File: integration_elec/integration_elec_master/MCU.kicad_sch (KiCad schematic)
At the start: 0 parts

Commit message: EM - Ajout des pages hiérarchiques pour le master, next : ajouter connecteurs pour les capteurs
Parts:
- added C1 (x2), C3 (x2), C5, C6, C7, C8, C9: 0.10uF, Capacitor_SMD:C_0805_2012Metric_Pad1.18x1.45mm_HandSolder, symbol Device:C_Small
- added C10: 4.7uF, Capacitor_SMD:C_0805_2012Metric_Pad1.18x1.45mm_HandSolder, symbol Device:C_Small
- added C11, C12: 10pF, Capacitor_SMD:C_0805_2012Metric_Pad1.18x1.45mm_HandSolder, symbol Device:C_Small
- added L1: FerritBead 600 OHM, Inductor_SMD:L_0805_2012Metric_Pad1.15x1.40mm_HandSolder, symbol Device:FerriteBead
- added R2, R3, R38: 10k, Resistor_SMD:R_0805_2012Metric_Pad1.20x1.40mm_HandSolder, symbol Device:R_US
- added R37: 120, Resistor_SMD:R_0805_2012Metric_Pad1.20x1.40mm_HandSolder, symbol Device:R_US
- added SW1: SW_Push, Button_Switch_SMD:SW_SPST_TL3342, symbol Switch:SW_Push
- added U3: STM32F446RETx, Package_QFP:LQFP-64_10x10mm_P0.5mm, symbol MCU_ST_STM32F4:STM32F446RETx
- added Y1: Crystal_16MHz, ab2_xtal:CSM-3X, symbol Device:Crystal
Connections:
- new net: R37.1, SW1.1
- new net: C10.2, C9.2, U3.30 (VCAP_1)
- new net: R2.1, U3.60 (BOOT0)
- new net: C6.2, L1.2, U3.13 (VDDA)
- new net: C11.1, U3.5 (PH0), Y1.1
- new net: C12.1, U3.6 (PH1), Y1.2
- new net: R3.2, U3.34 (PB13)
- new net +3V3: C1.1, C1.1, C3.1, C3.1, C5.1, C7.1, L1.1, R38.1, U3.1 (VBAT), U3.19 (VDD), U3.32 (VDD), U3.48 (VDD), U3.64 (VDD)
- new net DEBUG_NJTRST: U3.56 (PB4)
- new net DEBUG_RESET: C8.1, R38.2, SW1.2, U3.7 (NRST)
- new net DEBUG_SWCLK_TCK: U3.49 (PA14)
- new net DEBUG_SWDIO_TMS: U3.46 (PA13)
- new net DEBUG_SWO_TDI: U3.50 (PA15)
- new net DEBUG_SWO_TDO: U3.55 (PB3)
- new net DEBUG_UART_RX: U3.25 (PC5)
- new net DEBUG_UART_TX: U3.29 (PB10)
- new net GND: C1.2, C1.2, C10.1, C11.2, C12.2, C3.2, C3.2, C5.2, C6.1, C7.2, C8.2, C9.1, R2.2, R37.2, U3.12 (VSSA), U3.18 (VSS), U3.31 (VSS), U3.47 (VSS), U3.63 (VSS)
- new net RF.XBEE_LED: U3.24 (PC4)
- new net RF.XBEE_RQ: U3.41 (PA8)
- new net RF.XBEE_UART_CTS: U3.44 (PA11)
- new net RF.XBEE_UART_IN: U3.42 (PA9)
- new net RF.XBEE_UART_OUT: U3.43 (PA10)
- new net RF.XBEE_UART_RTS: U3.45 (PA12)
- new net USB_D+: U3.36 (PB15)
- new net USB_D-: U3.35 (PB14)
- new net USB_ID: U3.33 (PB12)
- new net USB_VBUS: R3.1
- no-connect marks 0 -> 5
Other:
- note added: "If the flash is blank, the bootloader will enable."
- note added: "RESET"
- note added: "Stabilization for the main regulator"

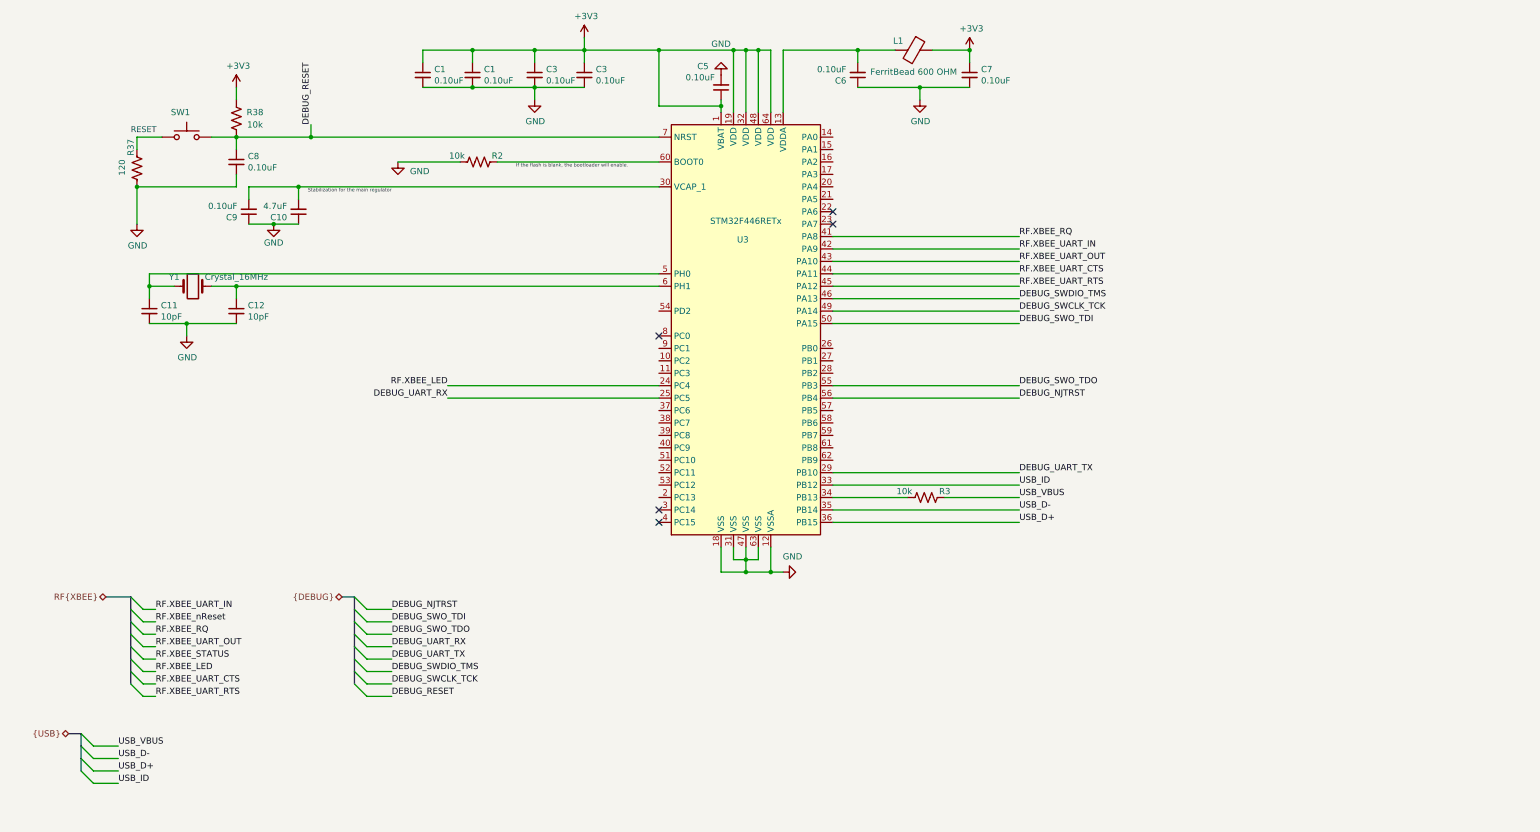
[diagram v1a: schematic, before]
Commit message: Added screen into schematic
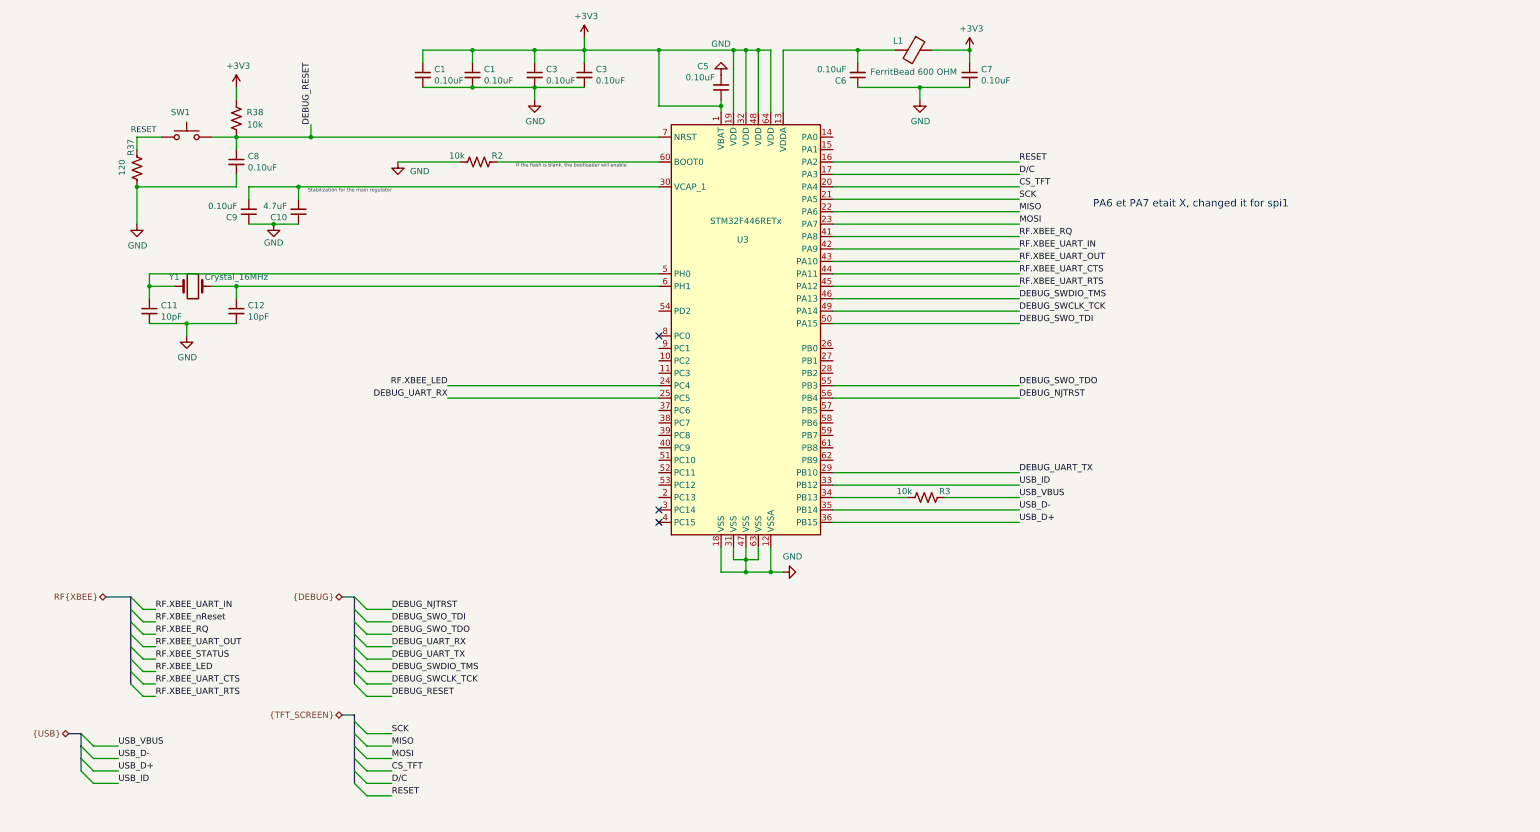
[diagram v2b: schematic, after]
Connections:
- net RESET: now reaches U3.16 (PA2)
- net D/C: now reaches U3.17 (PA3)
- net CS_TFT: now reaches U3.20 (PA4)
- net SCK: now reaches U3.21 (PA5)
- net MISO: now reaches U3.22 (PA6)
- net MOSI: now reaches U3.23 (PA7)
- no-connect marks 5 -> 3
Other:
- note added: "PA6 et PA7 etait X, changed it for spi1"

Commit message: Added footprint, symbol, 3D model for joystick. Added schematic for Joystick and comments
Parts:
- renumbered C1 to C11, C1 to C12, C3 to C13, C3 to C14, C5 to C15, C6 to C16, C7 to C17, C11 to C6, C8 to C7, C12 to C8, R37 to R5, R38 to R6, R2 to R7, R3 to R8, U3 to U2
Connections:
- net X_VALUE: now reaches U2.14 (PA0)
- net Y_VALUE: now reaches U2.15 (PA1)
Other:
- note added: "<- COULD BE PUT ON THE RESET, MIGHT BE BETTER..."

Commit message: Added plein de footprint
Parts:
- L1: footprint Inductor_SMD:L_0805_2012Metric_Pad1.15x1.40mm_HandSolder -> Inductor_SMD:L_0805_2012Metric_Pad1.05x1.20mm_HandSolder
- Y1: footprint ab2_xtal:CSM-3X -> JOYSTICK:XTAL_ECS-160-20-3X-TR
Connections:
- net VALVE_1: now reaches U2.39 (PC8)
- net VALVE_2: now reaches U2.40 (PC9)
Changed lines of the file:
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@@
 	)
 	(bus_entry
+		(at 30.48 138.43)
+		(size 2.54 2.54)
+		(stroke
+			(width 0)
+			(type default)
+		)
+	)
+	(bus_entry
 		(at 72.39 153.67)
 		(size 2.54 2.54)
@@
 	)
 	(bus_entry
-		(at 30.48 140.97)
+		(at 30.48 133.35)
 		(size 2.54 2.54)
 		(stroke
@@
 	)
 	(bus_entry
-		(at 30.48 143.51)
+		(at 30.48 135.89)
 		(size 2.54 2.54)
 		(stroke
@@
 	)
 	(bus_entry
+		(at 30.48 140.97)
+		(size 2.54 2.54)
+		(stroke
+			(width 0)
+			(type default)
+		)
+	)
+	(bus_entry
 		(at 72.39 161.29)
 		(size 2.54 2.54)
@@
 	(wire
 		(pts
+			(xy 102.87 114.3) (xy 146.05 114.3)
+		)
+		(stroke
+			(width 0)
+			(type default)
+		)
+	)
+	(wire
+		(pts
 			(xy 33.02 167.64) (xy 35.56 167.64)
 		)
@@
 	(wire
 		(pts
-			(xy 33.02 146.05) (xy 38.1 146.05)
+			(xy 33.02 138.43) (xy 38.1 138.43)
 		)
 		(stroke
@@
 	(wire
 		(pts
+			(xy 102.87 116.84) (xy 146.05 116.84)
+		)
+		(stroke
+			(width 0)
+			(type default)
+		)
+	)
+	(wire
+		(pts
 			(xy 33.02 154.94) (xy 35.56 154.94)
 		)
@@
 		)
 	)
+	(bus
+		(pts
+			(xy 30.48 138.43) (xy 30.48 140.97)
+		)
+		(stroke
+			(width 0)
+			(type default)
+		)
+	)
 	(wire
 		(pts
@@
 		)
 	)
+	(wire
+		(pts
+			(xy 33.02 140.97) (xy 38.1 140.97)
+		)
+		(stroke
+			(width 0)
+			(type default)
+		)
+	)
 	(bus
 		(pts
-			(xy 27.94 140.97) (xy 30.48 140.97)
+			(xy 27.94 133.35) (xy 30.48 133.35)
 		)
 		(stroke
@@
 	(wire
 		(pts
+			(xy 33.02 143.51) (xy 38.1 143.51)
+		)
+		(stroke
+			(width 0)
+			(type default)
+		)
+	)
+	(wire
+		(pts
 			(xy 74.93 151.13) (xy 80.01 151.13)
 		)
@@
 	(wire
 		(pts
-			(xy 33.02 143.51) (xy 38.1 143.51)
+			(xy 33.02 135.89) (xy 38.1 135.89)
 		)
 		(stroke
@@
 	(bus
 		(pts
-			(xy 30.48 140.97) (xy 30.48 143.51)
+			(xy 30.48 133.35) (xy 30.48 135.89)
 		)
 		(stroke
@@
 		)
 	)
+	(bus
+		(pts
+			(xy 30.48 135.89) (xy 30.48 138.43)
+		)
+		(stroke
+			(width 0)
+			(type default)
+		)
+	)
 	(wire
 		(pts
@@
 	)
 	(label "X_VALUE"
-		(at 38.1 143.51 0)
+		(at 38.1 135.89 0)
 		(effects
 			(font
@@
 		)
 	)
+	(label "VALVE_2"
+		(at 102.87 116.84 180)
+		(effects
+			(font
+				(size 1.27 1.27)
+			)
+			(justify right bottom)
+		)
+	)
 	(label "Y_VALUE"
-		(at 38.1 146.05 0)
+		(at 38.1 138.43 0)
 		(effects
 			(font
@@
 		)
 	)
+	(label "VALVE_1"
+		(at 102.87 114.3 180)
+		(effects
+			(font
+				(size 1.27 1.27)
+			)
+			(justify right bottom)
+		)
+	)
 	(label "DEBUG_SWCLK_TCK"
 		(at 219.71 88.9 0)
@@
 		)
 	)
+	(label "VALVE_1"
+		(at 38.1 140.97 0)
+		(effects
+			(font
+				(size 1.27 1.27)
+			)
+			(justify left bottom)
+		)
+	)
 	(label "DEBUG_UART_TX"
 		(at 219.71 121.92 0)
@@
 		)
 	)
+	(label "VALVE_2"
+		(at 38.1 143.51 0)
+		(effects
+			(font
+				(size 1.27 1.27)
+			)
+			(justify left bottom)
+		)
+	)
 	(label "DEBUG_SWDIO_TMS"
 		(at 219.71 86.36 0)
@@
 	(hierarchical_label "{JOYSTICK}"
 		(shape bidirectional)
-		(at 27.94 140.97 180)
+		(at 27.94 133.35 180)
 		(effects
 			(font
@@
 			)
 		)
-		(property "Footprint" "Inductor_SMD:L_0805_2012Metric_Pad1.15x1.40mm_HandSolder"
+		(property "Footprint" "Inductor_SMD:L_0805_2012Metric_Pad1.05x1.20mm_HandSolder"
 			(at 198.12 33.782 90)
 			(effects
@@
 			)
 		)
-		(property "Footprint" "ab2_xtal:CSM-3X"
+		(property "Footprint" "JOYSTICK:XTAL_ECS-160-20-3X-TR"
 			(at 50.8 83.82 0)
 			(effects

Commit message: Added comment for pull-down
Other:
- note added: "PC8 AND PC9 NEEDS TO BE PULL-DOWN"
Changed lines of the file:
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@@
 	(generator_version "9.0")
 	(paper "A4")
+	(text "PC8 AND PC9 NEEDS TO BE PULL-DOWN\n"
+		(exclude_from_sim no)
+		(at 69.596 114.554 0)
+		(effects
+			(font
+				(size 1.27 1.27)
+			)
+		)
+	)
 	(text "RESET"
 		(exclude_from_sim no)

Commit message: KAH - Fini schematic attente de review + correction BUS
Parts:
- added R10, R5: 0, Resistor_SMD:R_0805_2012Metric_Pad1.20x1.40mm_HandSolder, symbol Device:R_US
- renumbered R5 to R6, R6 to R7, R7 to R8, R8 to R9
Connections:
- net RF.XBEE_STATUS: now also U2.40 (PC9)
- net RF.XBEE_nReset: now also U2.51 (PC10)
- net VALVE_1: now also U2.38 (PC7); no longer U2.39 (PC8)
- net VALVE_2: now also U2.39 (PC8); no longer U2.40 (PC9)
- net at R6.1, SW1.1: now also R5.2
- net DEBUG_SWCLK_TCK renamed DEBUG_SWCLK
- net DEBUG_SWDIO_TMS renamed DEBUG_SWDIO
- net RESET: no longer names the net of U2.16 (PA2)
- net RESET: now also R10.1
- net USB_ID: no longer names the net of U2.33 (PB12)
- net X_VALUE: no longer names the net of U2.14 (PA0)
- net Y_VALUE: no longer names the net of U2.15 (PA1)
- new net RESET_TFT: R10.2, R5.1
- no-connect marks 3 -> 22

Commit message: KAH - added the part # for some pieces. MISSING R NC and USB-C conn
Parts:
- R10, R5: DigiKey (none) -> RMCF0805ZT0R00CT-ND
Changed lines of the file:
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@@
+			)
+		)
+		(property "DigiKey" "RMCF0805ZT0R00CT-ND"
+			(at 26.67 53.34 90)
+			(effects
+				(font
+					(size 1.27 1.27)
+				)
+				(hide yes)
 			)
 		)
@@
 			(effects
 				(font
+					(size 1.27 1.27)
+				)
+				(hide yes)
+			)
+		)
+		(property "DigiKey" "RMCF0805ZT0R00CT-ND"
+			(at 233.68 58.42 90)
+			(effects
+				(font

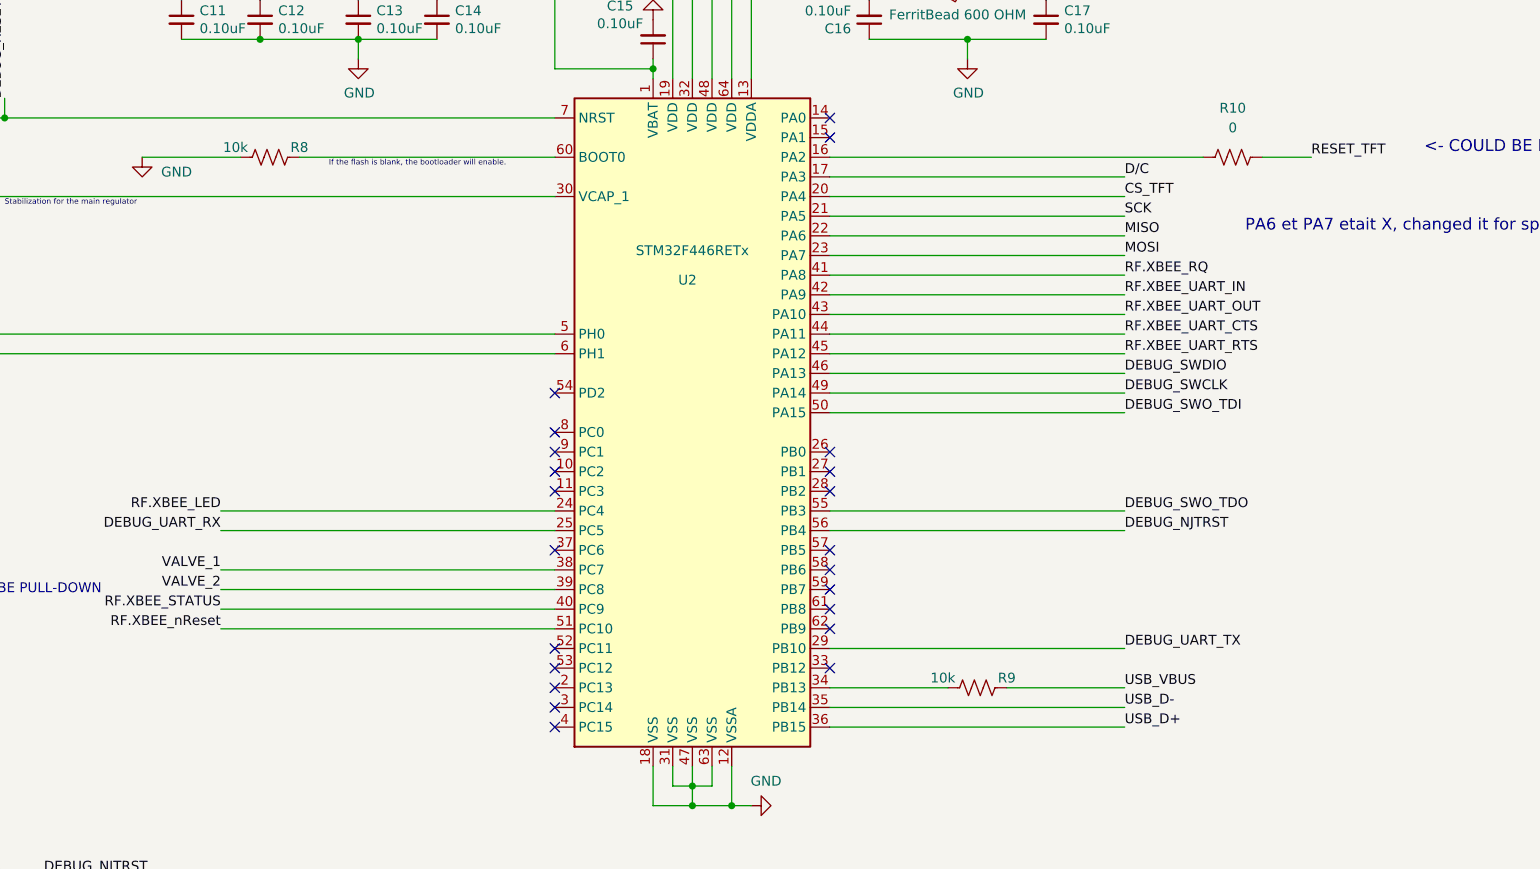
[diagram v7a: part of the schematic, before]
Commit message: KAH - commencer le setup de MXCube, added files for the screen
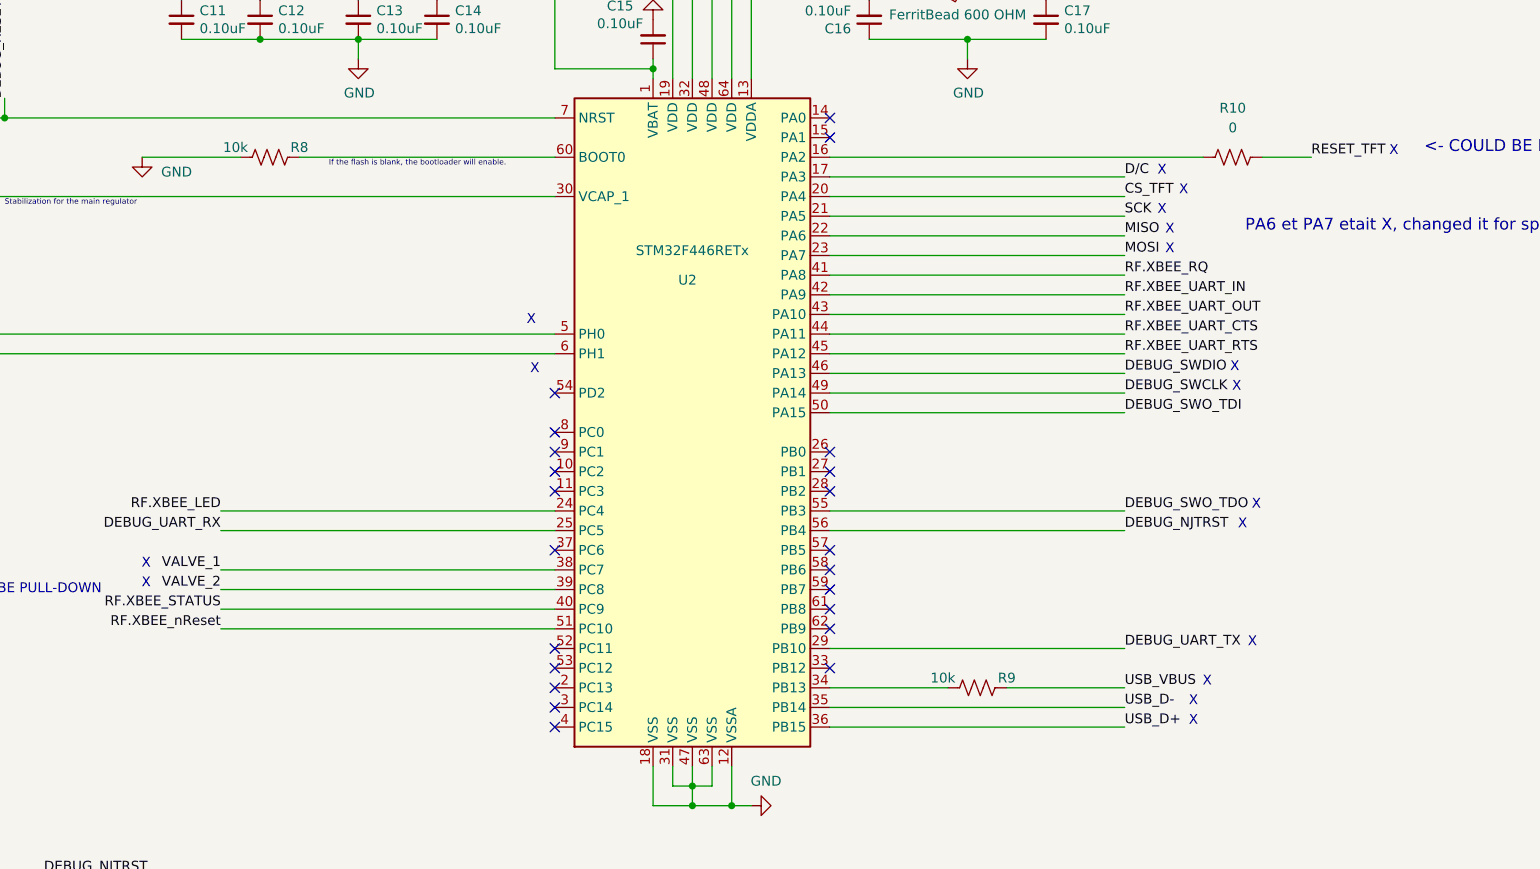
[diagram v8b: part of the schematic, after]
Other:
- note added: "X"
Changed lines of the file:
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@@
+		)
+	)
+	(text "X"
+		(exclude_from_sim no)
+		(at 234.188 88.138 0)
+		(effects
+			(font
+				(size 1.27 1.27)
+				(color 255 0 32 1)
+			)
 		)
 	)
@@
 		)
 	)
+	(text "X"
+		(exclude_from_sim no)
+		(at 228.6 128.778 0)
+		(effects
+			(font
+				(size 1.27 1.27)
+				(color 255 0 32 1)
+			)
+		)
+	)
+	(text "X"
+		(exclude_from_sim no)
+		(at 228.6 131.318 0)
+		(effects
+			(font
+				(size 1.27 1.27)
+				(color 255 0 32 1)
+			)
+		)
+	)
 	(text "RESET"
 		(exclude_from_sim no)
@@
 			)
 			(justify left bottom)
+		)
+	)
+	(text "X"
+		(exclude_from_sim no)
+		(at 225.552 67.818 0)
+		(effects
+			(font
+				(size 1.27 1.27)
+				(color 255 0 32 1)
+			)
+		)
+	)
+	(text "X"
+		(exclude_from_sim no)
+		(at 143.002 79.502 0)
+		(effects
+			(font
+				(size 1.27 1.27)
+				(color 255 0 32 1)
+			)
+		)
+	)
+	(text "X"
+		(exclude_from_sim no)
+		(at 236.22 121.158 0)
+		(effects
+			(font
+				(size 1.27 1.27)
+				(color 255 0 32 1)
+			)
+		)
+	)
+	(text "X"
+		(exclude_from_sim no)
+		(at 224.536 65.278 0)
+		(effects
+			(font
+				(size 1.27 1.27)
+				(color 255 0 32 1)
+			)
+		)
+	)
+	(text "X"
+		(exclude_from_sim no)
+		(at 227.33 62.738 0)
+		(effects
+			(font
+				(size 1.27 1.27)
+				(color 255 0 32 1)
+			)
+		)
+	)
+	(text "X"
+		(exclude_from_sim no)
+		(at 236.728 103.378 0)
+		(effects
+			(font
+				(size 1.27 1.27)
+				(color 255 0 32 1)
+			)
+		)
+	)
+	(text "X"
+		(exclude_from_sim no)
+		(at 233.934 85.598 0)
+		(effects
+			(font
+				(size 1.27 1.27)
+				(color 255 0 32 1)
+			)
 		)
 	)
@@
 			)
 		)
+	)
+	(text "X"
+		(exclude_from_sim no)
+		(at 224.536 60.198 0)
+		(effects
+			(font
+				(size 1.27 1.27)
+				(color 255 0 32 1)
+			)
+		)
+	)
+	(text "X"
+		(exclude_from_sim no)
+		(at 230.378 126.238 0)
+		(effects
+			(font
+				(size 1.27 1.27)
+				(color 255 0 32 1)
+			)
+		)
+	)
+	(text "X"
+		(exclude_from_sim no)
+		(at 143.4623 85.852 0)
+		(effects
+			(font
+				(size 1.27 1.27)
+				(color 255 0 32 1)
+			)
+		)
+	)
+	(text "X"
+		(exclude_from_sim no)
+		(at 234.95 105.918 0)
+		(effects
+			(font
+				(size 1.27 1.27)
+				(color 255 0 32 1)
+			)
+		)
+	)
+	(text "X"
+		(exclude_from_sim no)
+		(at 93.218 113.538 0)
+		(effects
+			(font
+				(size 1.27 1.27)
+				(color 255 0 32 1)
+			)
+		)
+	)
+	(text "X"
+		(exclude_from_sim no)
+		(at 93.218 110.998 0)
+		(effects
+			(font
+				(size 1.27 1.27)
+				(color 255 0 32 1)
+			)
+		)
+	)
+	(text "X"
+		(exclude_from_sim no)
+		(at 225.552 70.358 0)
+		(effects
+			(font
+				(size 1.27 1.27)
+				(color 255 0 32 1)
+			)
+		)
+	)
+	(text "X"
+		(exclude_from_sim no)
+		(at 254.508 57.658 0)
+		(effects
+			(font
+				(size 1.27 1.27)
+				(color 255 0 32 1)
+			)
+		)
